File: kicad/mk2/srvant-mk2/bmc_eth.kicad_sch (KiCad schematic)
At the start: 84 parts, among them J5 ARJM11, U10 TPD4EUSB30, U11 TPD4EUSB30, U12 KSZ9131RNXI-TR, U5 rp-t113-s3, Y2 25Mhz

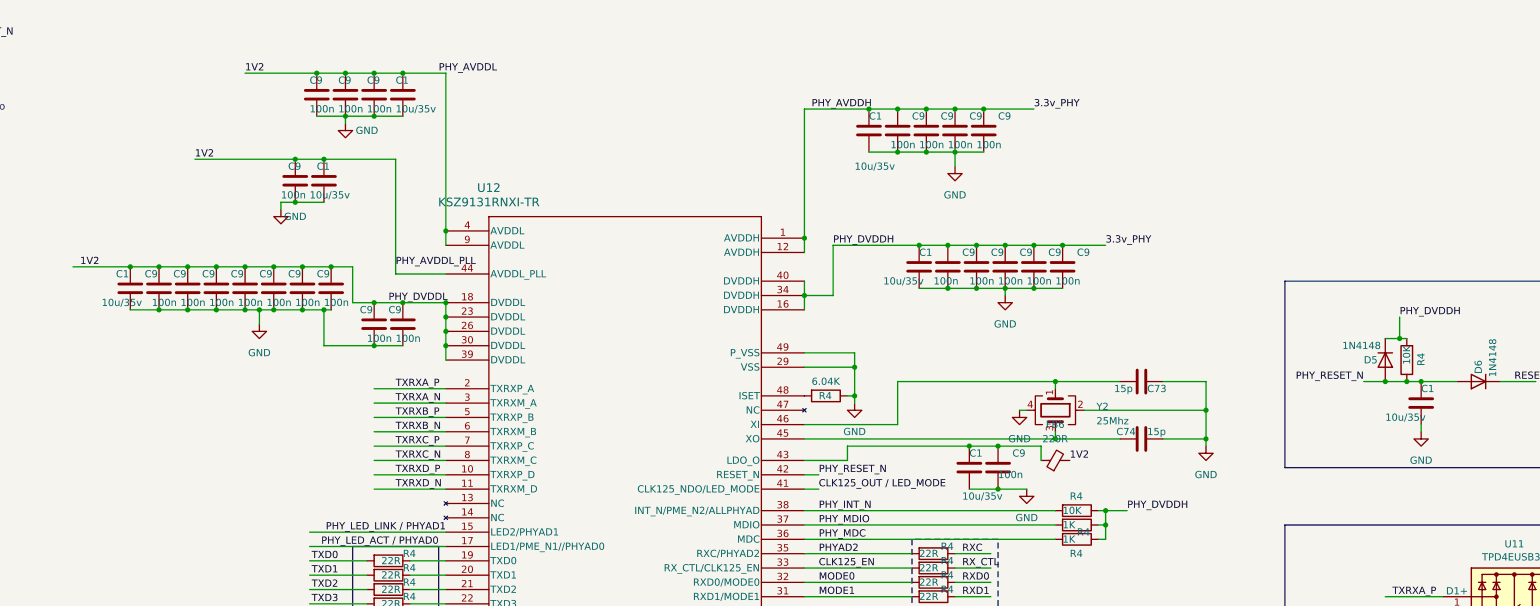
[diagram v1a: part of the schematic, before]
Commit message: fix descriptions, add 3dmodels.
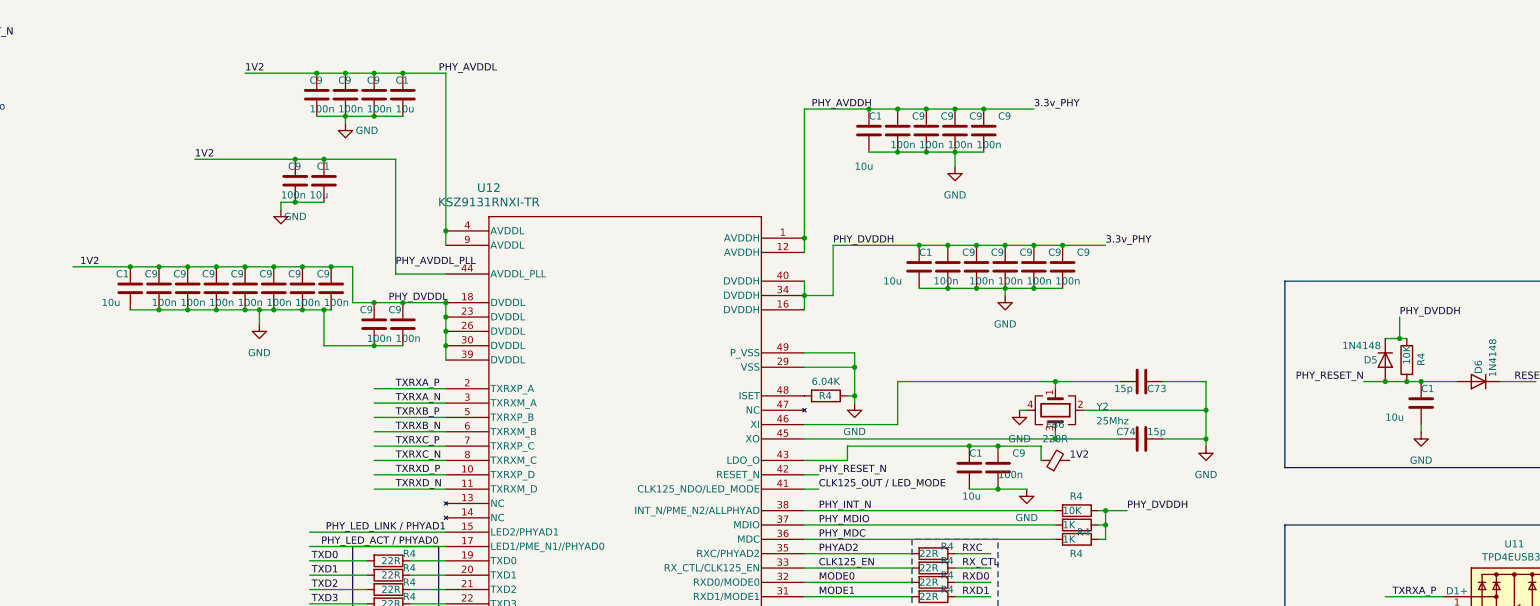
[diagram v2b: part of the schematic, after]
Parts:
- C1: value 10u/35v -> 10u
- C9: Part Description 0.1uF 10% 16V Ceramic Capacitor X7R 0402 (1005 Metric) -> 0.1uF 10% 16V Ceramic Capacitor X7R 0402 (1005 Metric)

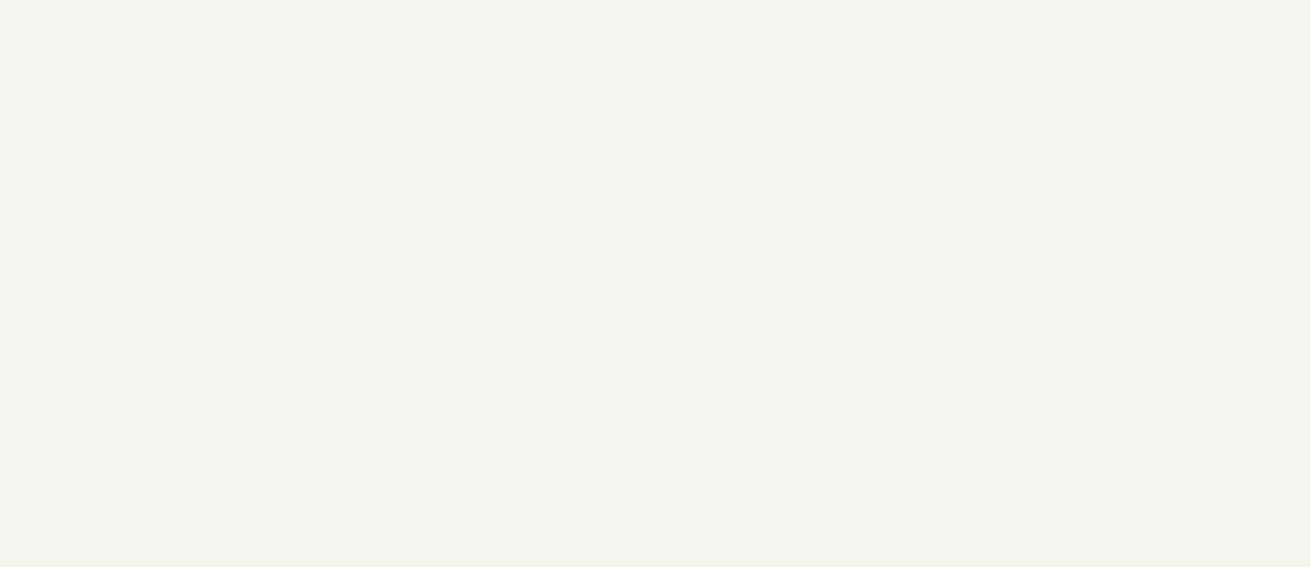
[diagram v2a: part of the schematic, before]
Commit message: replace power jack, change board dimentions, small fixes
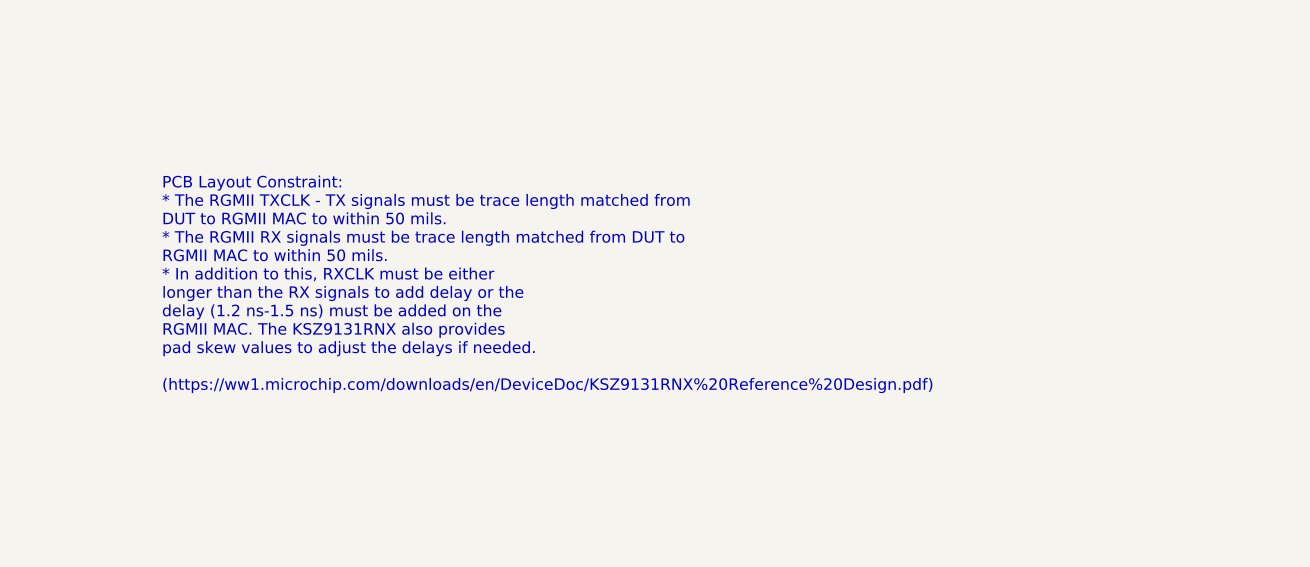
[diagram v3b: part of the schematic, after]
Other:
- note added: "PCB Layout Constraint: * The RGMII TXCLK - TX signals must be trace length matched from DUT to RGMII MAC to within 50 mils. * The RGMII RX signals must be trace length matched from DUT to RGMII MAC to within 50 mils. * In addition to this, RXCLK must be either longer than the RX signals to add delay or the delay (1.2 ns-1.5 ns) must be added on the RGMII MAC. The KSZ9131RNX also provides pad skew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"
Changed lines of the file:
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@@
+    (effects (font (size 1.27 1.27)) (justify left bottom))
+  )
+  (text "PCB Layout Constraint: \n* The RGMII TXCLK - TX signals must be trace length matched from\nDUT to RGMII MAC to within 50 mils.\n* The RGMII RX signals must be trace length matched from DUT to\nRGMII MAC to within 50 mils.\n* In addition to this, RXCLK must be either\nlonger than the RX signals to add delay or the\ndelay (1.2 ns-1.5 ns) must be added on the\nRGMII MAC. The KSZ9131RNX also provides\npad skew values to adjust the delays if needed.\n\n(https://ww1.microchip.com/downloads/en/DeviceDoc/KSZ9131RNX%20Reference%20Design.pdf)"
+    (at 433.07 191.77 0)
     (effects (font (size 1.27 1.27)) (justify left bottom))
   )

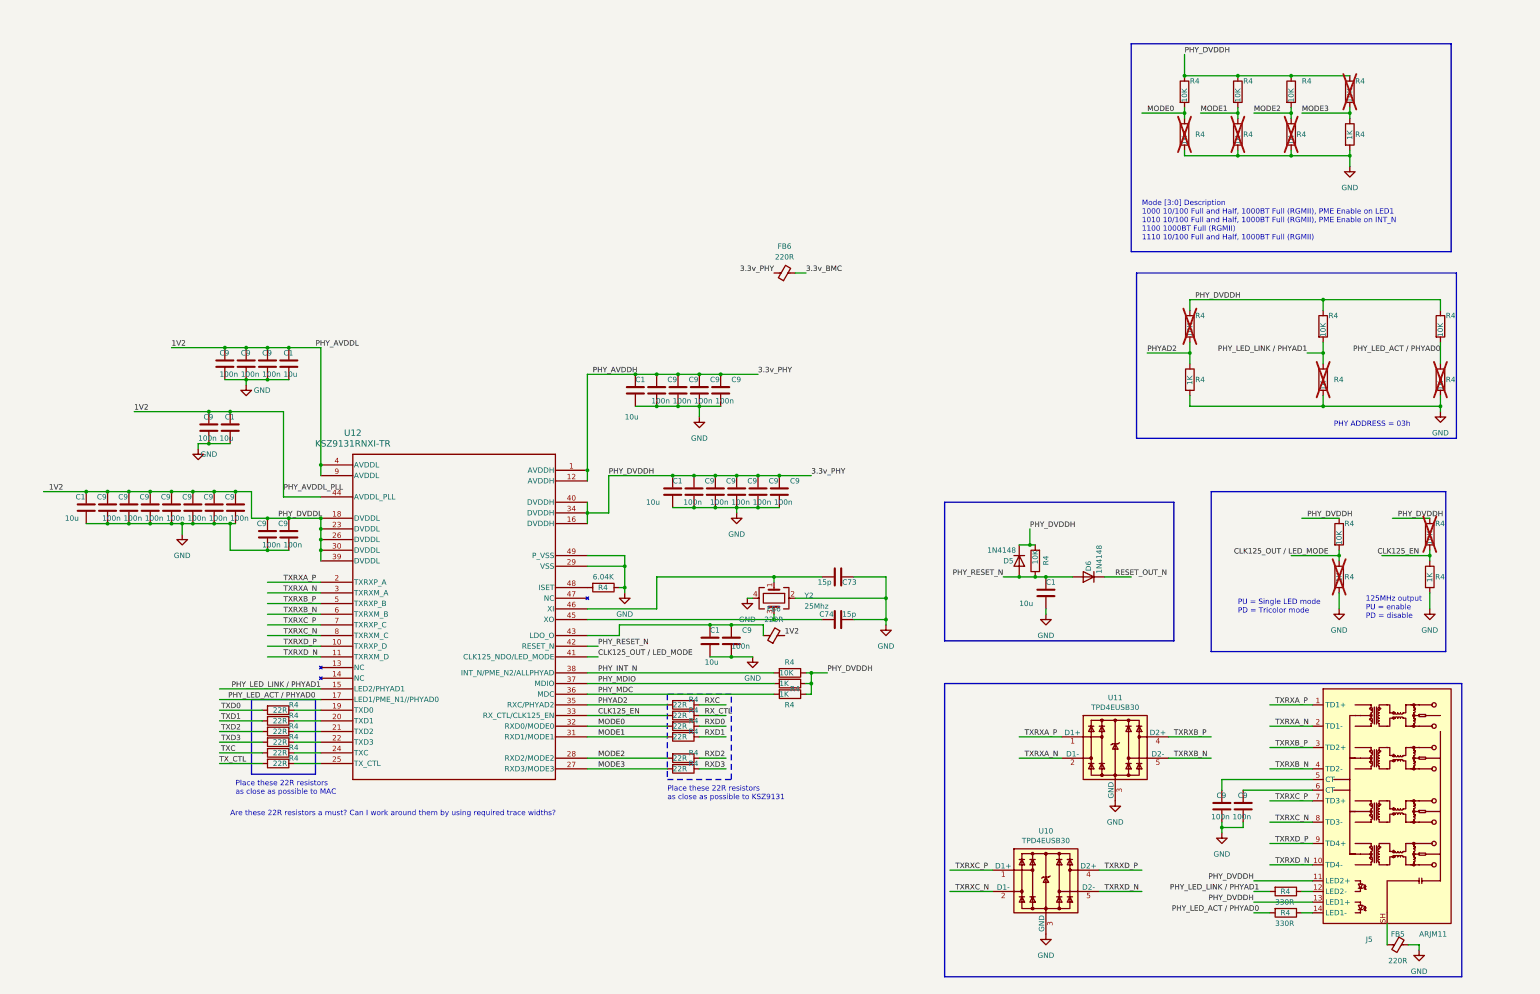
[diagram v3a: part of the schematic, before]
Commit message: add rp-t113-s3 datasheets (cn), make CI happier
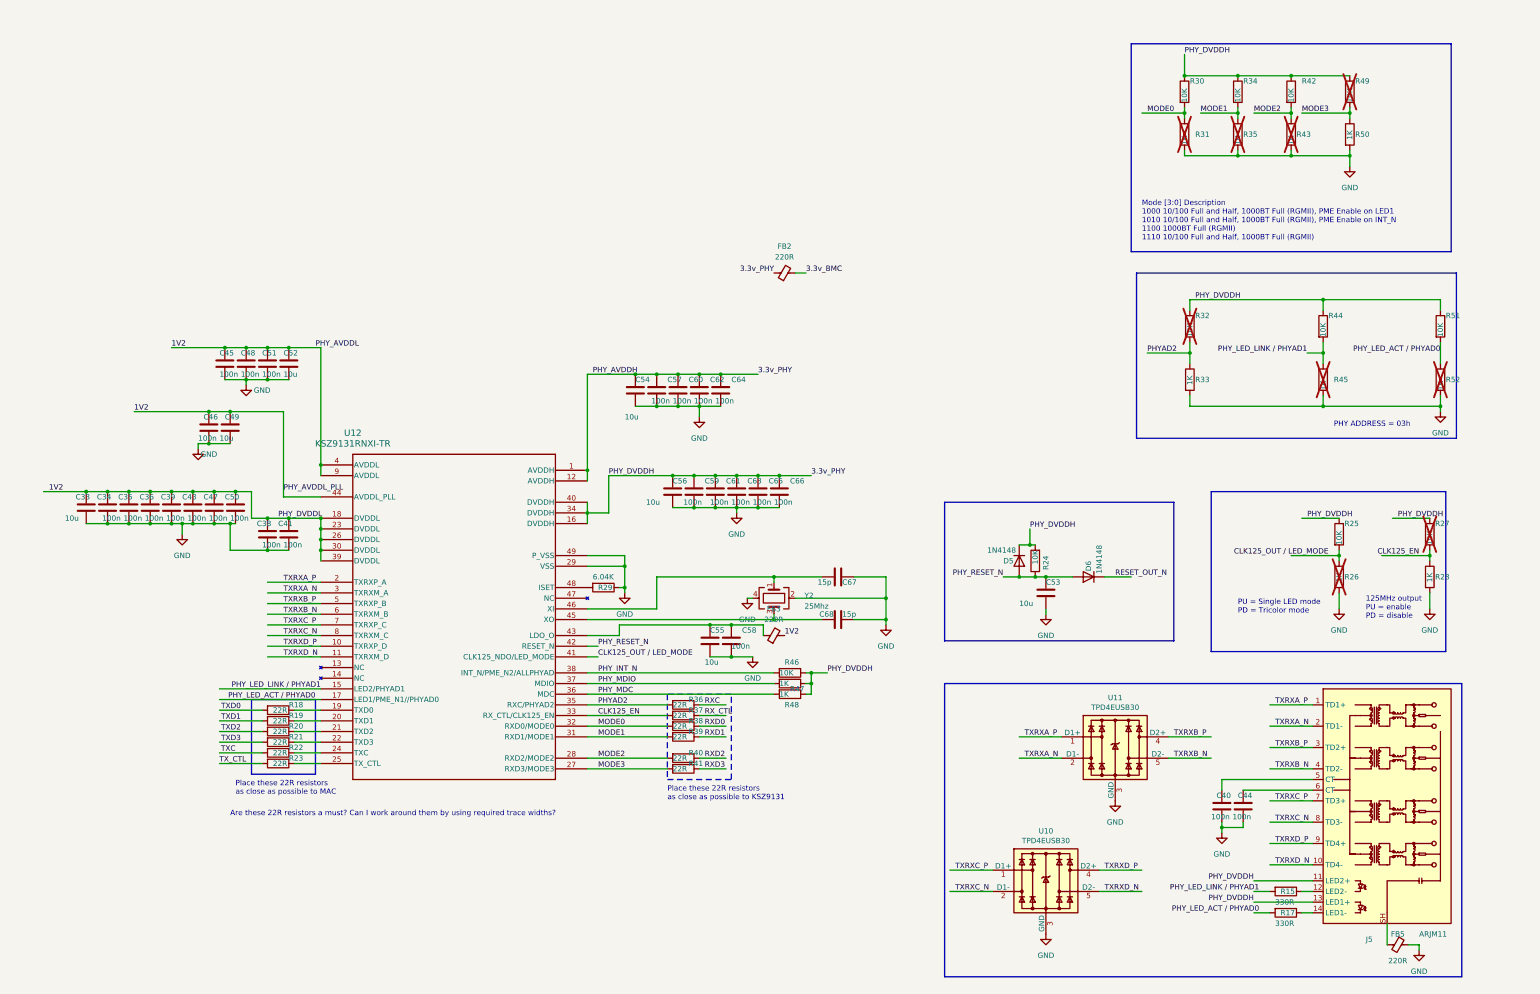
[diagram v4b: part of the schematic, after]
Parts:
- C33, C49, C52, C53, C54, C55, C56: renamed from C1; manf# GRM21BC8YA106KE11L -> GRM21BC8YA106KE11L
- C34, C35, C36, C38, C39, C40, C41, C43, C44, C45, C46, C47, C48, C50, C51, C57, C58, C59, C60, C61, C62, C63, C64, C65, C66: renamed from C9; mouser# 963-EMK105B7104KV-F -> 963-EMK105B7104KV-F
- FB2, FB3: renamed from FB6; manf# BLM15PX221SH1D -> BLM15PX221SH1D; mouser# 81-BLM15PX221SH1D -> 81-BLM15PX221SH1D
- FB5: manf# BLM15PX221SH1D -> BLM15PX221SH1D; mouser# 81-BLM15PX221SH1D -> 81-BLM15PX221SH1D
- R26, R28, R31, R33, R35, R43, R45, R47, R48, R50, R52: renamed from R4; Part Description (none) -> Resistor 1K M1005 1% 63mW
- renumbered C73 to C67, C74 to C68, R4 to R15, R4 to R17, R4 to R18, R4 to R19, R4 to R20, R4 to R21, R4 to R22, R4 to R23, R4 to R24, R4 to R25, R4 to R27, R4 to R29, R4 to R30, R4 to R32, R4 to R34, R4 to R36, R4 to R37, R4 to R38, R4 to R39, R4 to R40, R4 to R41, R4 to R42, R4 to R44, R4 to R46, R4 to R49, R4 to R51

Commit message: fix 3d models. again
Once again assign all the 3d models to the components.
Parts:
- U5: footprint rp-t113-s3:rp-t113-s3 -> footprints:rp-t113-s3
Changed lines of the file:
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@@
       (effects (font (size 1.27 1.27)))
     )
-    (property "Footprint" "rp-t113-s3:rp-t113-s3" (at 5.08 41.91 0)
+    (property "Footprint" "footprints:rp-t113-s3" (at 5.08 41.91 0)
       (effects (font (size 1.27 1.27)) hide)
     )

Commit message: lot's of small updates
* fix the quartz footprint
* fix wrong inductor in pcie power unit
* fix lots of descriptions,uids
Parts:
- C67, C68: Part Description (none) -> SMD Multilayer Ceramic Capacitor, 15 pF, 16 V, 0402 [1005 M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; farnell# (none) -> 2627389; manf# (none) -> MC0402N150J160CT
- D5, D6: farnell# (none) -> 1773531
- FB2, FB3, FB5: farnell# (none) -> 4236024
- R29: farnell# (none) -> 3495661; manf# (none) -> RC0402FR-076K04L
- Y2: footprint footprints:LFXTAL-25MHz -> PCM_Crystal_AKL:Crystal_SMD_FOX_FQ7050-4Pin_7.0x5.0mm
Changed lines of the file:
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@@
       (effects (font (size 1.27 1.27)) hide)
     )
-    (property "manf#" "" (at 200.66 152.4 0)
+    (property "manf#" "RC0402FR-076K04L" (at 200.66 152.4 0)
       (effects (font (size 1.27 1.27)) hide)
     )
@@
       (effects (font (size 1.27 1.27)) hide)
     )
-    (property "farnell#" "" (at 200.66 152.4 0)
+    (property "farnell#" "3495661" (at 200.66 152.4 0)
       (effects (font (size 1.27 1.27)) hide)
     )
@@
       (effects (font (size 1.27 1.27)) hide)
     )
-    (property "farnell#" "" (at 243.84 77.47 0)
+    (property "farnell#" "4236024" (at 243.84 77.47 0)
       (effects (font (size 1.27 1.27)) hide)
     )
@@
       (effects (font (size 1.27 1.27)) hide)
     )
-    (property "farnell#" "" (at 389.89 237.49 0)
+    (property "farnell#" "4236024" (at 389.89 237.49 0)
       (effects (font (size 1.27 1.27)) hide)
     )
@@
       (effects (font (size 1.27 1.27)) hide)
     )
-    (property "Datasheet" "~{}" (at 256.54 160.02 0)
+    (property "Datasheet" "https://4donline.ihs.com/images/VipMasterIC/IC/SCMP/SCMP-S-A0009426256/SCMP-S-A0009474646-1.pdf" (at 256.54 160.02 0)
       (effects (font (size 1.27 1.27)) hide)
     )
-    (property "manf#" "" (at 256.54 160.02 0)
+    (property "manf#" "MC0402N150J160CT" (at 256.54 160.02 0)
       (effects (font (size 1.27 1.27)) hide)
     )
@@
       (effects (font (size 1.27 1.27)) hide)
     )
-    (property "farnell#" "" (at 256.54 160.02 0)
+    (property "farnell#" "2627389" (at 256.54 160.02 0)
       (effects (font (size 1.27 1.27)) hide)
     )
@@
       (effects (font (size 1.27 1.27)) hide)
     )
-    (property "Part Description" "" (at 256.54 160.02 0)
+    (property "Part Description" "SMD Multilayer Ceramic Capacitor, 15 pF, 16 V, 0402 [1005 Metric], ± 5%, C0G / NP0, MC" (at 256.54 160.02 0)
       (effects (font (size 1.27 1.27)) hide)
     )
@@
       (effects (font (size 1.27 1.27)) hide)
     )
-    (property "farnell#" "" (at 299.72 146.05 0)
+    (property "farnell#" "1773531" (at 299.72 146.05 0)
       (effects (font (size 1.27 1.27)) hide)
     )
@@
       (effects (font (size 1.27 1.27)) hide)
     )
-    (property "farnell#" "" (at 316.23 149.86 0)
+    (property "farnell#" "1773531" (at 316.23 149.86 0)
       (effects (font (size 1.27 1.27)) hide)
     )
@@
       (effects (font (size 1.27 1.27)) hide)
     )
-    (property "Datasheet" "~{}" (at 256.54 149.86 0)
+    (property "Datasheet" "https://4donline.ihs.com/images/VipMasterIC/IC/SCMP/SCMP-S-A0009426256/SCMP-S-A0009474646-1.pdf" (at 256.54 149.86 0)
       (effects (font (size 1.27 1.27)) hide)
     )
-    (property "manf#" "" (at 256.54 149.86 0)
+    (property "manf#" "MC0402N150J160CT" (at 256.54 149.86 0)
       (effects (font (size 1.27 1.27)) hide)
     )
@@
       (effects (font (size 1.27 1.27)) hide)
     )
-    (property "farnell#" "" (at 256.54 149.86 0)
+    (property "farnell#" "2627389" (at 256.54 149.86 0)
       (effects (font (size 1.27 1.27)) hide)
     )
@@
       (effects (font (size 1.27 1.27)) hide)
     )
-    (property "Part Description" "" (at 256.54 149.86 0)
+    (property "Part Description" "SMD Multilayer Ceramic Capacitor, 15 pF, 16 V, 0402 [1005 Metric], ± 5%, C0G / NP0, MC" (at 256.54 149.86 0)
       (effects (font (size 1.27 1.27)) hide)
     )
@@
       (effects (font (size 1.27 1.27)) hide)
     )
-    (property "farnell#" "" (at 241.3 163.83 0)
+    (property "farnell#" "4236024" (at 241.3 163.83 0)
       (effects (font (size 1.27 1.27)) hide)
     )
@@
       (effects (font (size 1.27 1.27)) (justify left))
     )
-    (property "Footprint" "footprints:LFXTAL-25MHz" (at 241.3 154.94 0)
+    (property "Footprint" "PCM_Crystal_AKL:Crystal_SMD_FOX_FQ7050-4Pin_7.0x5.0mm" (at 241.3 154.94 0)
       (effects (font (size 1.27 1.27)) hide)
     )

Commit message: fix variable substitution
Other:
- title: (none) -> srvant mk2
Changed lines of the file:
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@@
 (kicad_sch (version 20230121) (generator eeschema)
   (paper "A3")
+  (title_block
+    (title "srvant mk2")
+    (rev "${git_hash}")
+  )
   (junction (at 107.95 129.54) (diameter 0) (color 0 0 0 0)
   )
